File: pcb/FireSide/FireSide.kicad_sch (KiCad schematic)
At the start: 24 parts, among them J1 XT60-Male, J10 Screw_Terminal_Status_LED, J2 Spring_Terminal_Sensor_5V, J3 Spring_Terminal_Sensor_GND, J4 Screw_Terminal_Igniter_A, J5 Screw_Terminal_Igniter_B, J6 Spring_Terminal_A1toA3_SIG, J7 Spring_Terminal_A4toA6_SIG, J8 Spring_Terminal_A1toA3_GND, J9 Spring_Terminal_A4toA6_GND, Q1 BC557, Q2 IRLZ44N, Q3 BC557, Q4 IRLZ44N, Q5 2N2222, U1 LM7805ABV

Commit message: [FS] Create PCB Board Design
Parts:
- removed Q1, Q3: BC557, Package_TO_SOT_THT:TO-92_HandSolder, symbol Transistor_BJT:BC557
- removed Q5: 2N2222, Package_TO_SOT_THT:TO-92L_HandSolder, symbol Device:Q_NPN
- added Q1, Q3, Q5: 2N2222, Package_TO_SOT_THT:TO-92_HandSolder, symbol Transistor_BJT:PN2222A
- J1: footprint Connector_AMASS:AMASS_XT60-M_1x02_P7.20mm_Vertical -> XT60-M:AMASS_XT60-M
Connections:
- net +BATT: now also R2.1, R3.1
- net FIRE_PIN_A: now also Q1.2 (B)
- net FIRE_PIN_B: now also Q3.2 (B)
- net GND: now also Q1.1 (E), Q3.1 (E), Q5.1 (E); no longer R2.2, R3.2
- net STATUS_PIN: now also Q5.2 (B)
- net at Q2.1 (G): now also R2.2, Q1.3 (C); no longer R2.1
- net at Q4.1 (G): now also R3.2, Q3.3 (C); no longer R3.1
- net at R4.2: now also Q5.3 (C)
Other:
- moved on the sheet: R2

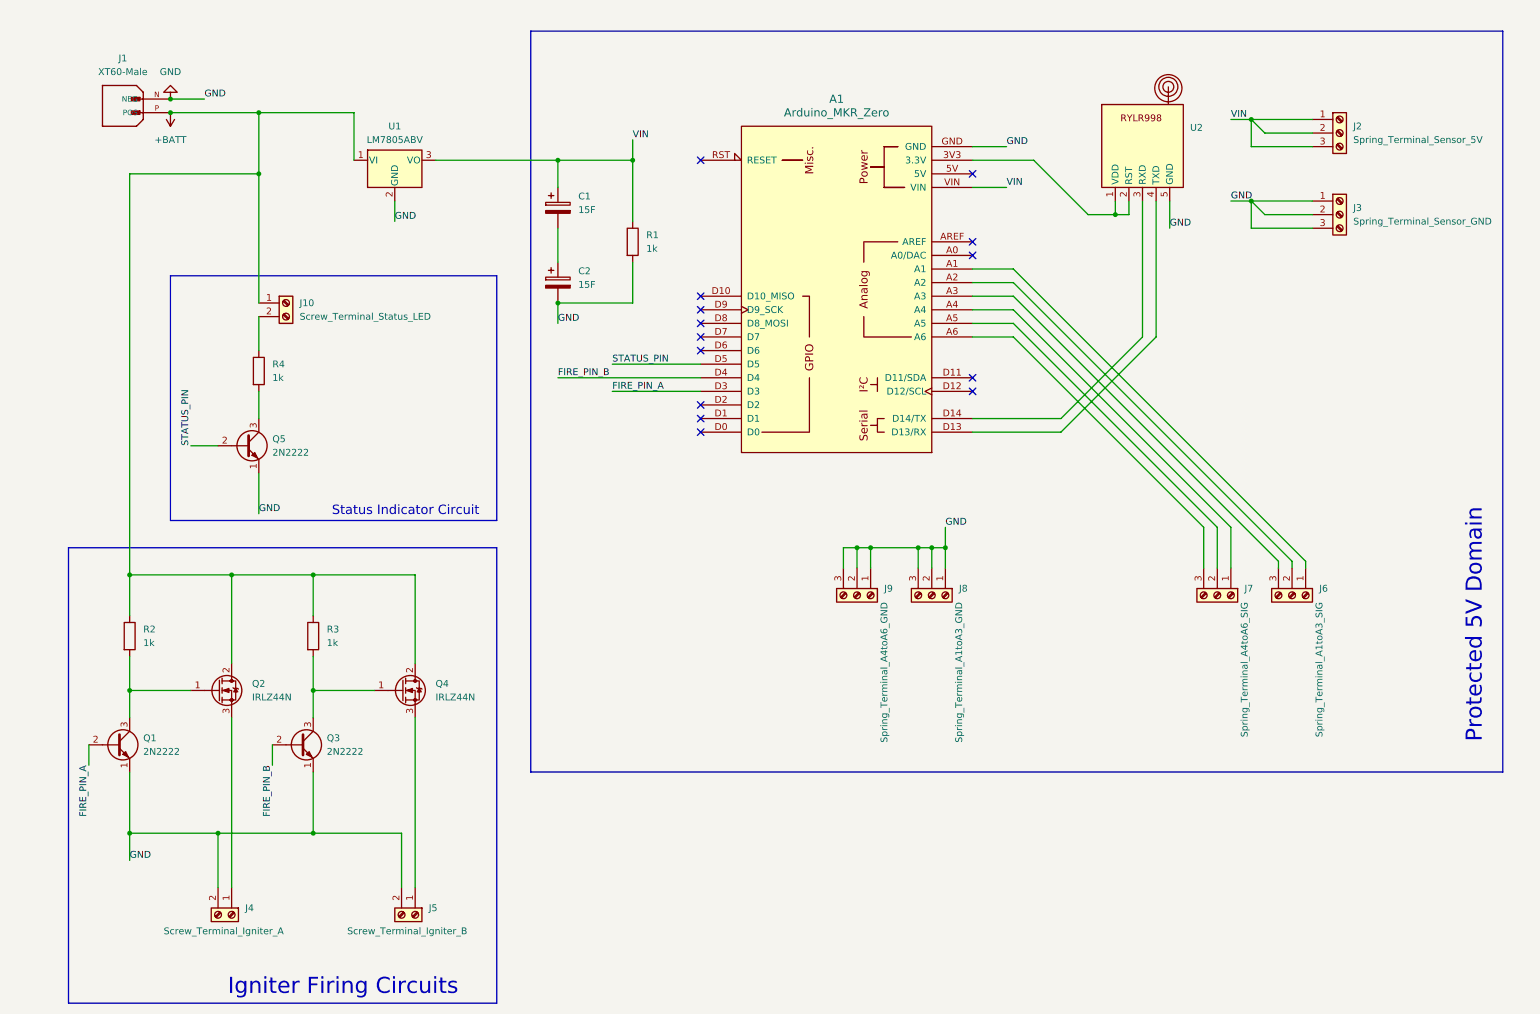
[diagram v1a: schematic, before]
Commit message: [FS] Update PCB to 120x80 mm and Use JST Connectors
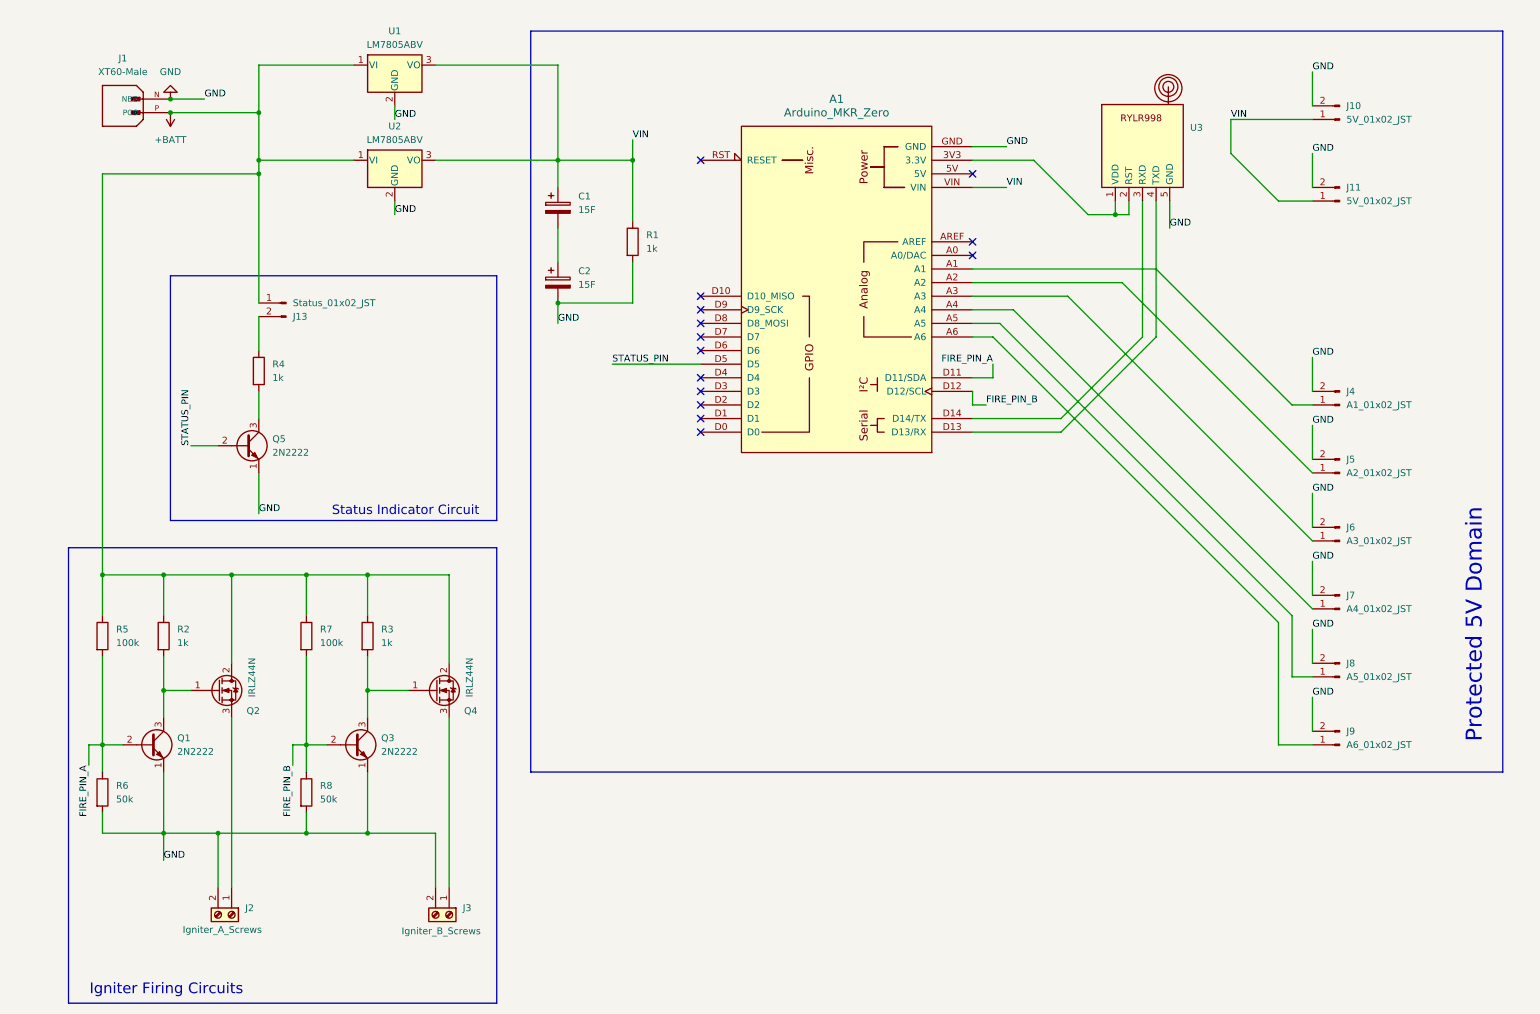
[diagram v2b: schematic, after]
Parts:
- removed J10: Screw_Terminal_Status_LED, TerminalBlock_MetzConnect:TerminalBlock_MetzConnect_Type059_RT06302HBWC_1x02_P3.50mm_Horizontal, symbol Connector:Screw_Terminal_01x02
- removed J2: Spring_Terminal_Sensor_5V, TerminalBlock_MetzConnect:TerminalBlock_MetzConnect_Type011_RT05503HBLC_1x03_P5.00mm_Horizontal, symbol Connector:Screw_Terminal_01x03
- removed J3: Spring_Terminal_Sensor_GND, TerminalBlock_MetzConnect:TerminalBlock_MetzConnect_Type011_RT05503HBLC_1x03_P5.00mm_Horizontal, symbol Connector:Screw_Terminal_01x03
- removed J6: Spring_Terminal_A1toA3_SIG, TerminalBlock_MetzConnect:TerminalBlock_MetzConnect_Type011_RT05503HBLC_1x03_P5.00mm_Horizontal, symbol Connector:Screw_Terminal_01x03
- removed J7: Spring_Terminal_A4toA6_SIG, TerminalBlock_MetzConnect:TerminalBlock_MetzConnect_Type011_RT05503HBLC_1x03_P5.00mm_Horizontal, symbol Connector:Screw_Terminal_01x03
- removed J8: Spring_Terminal_A1toA3_GND, TerminalBlock_MetzConnect:TerminalBlock_MetzConnect_Type011_RT05503HBLC_1x03_P5.00mm_Horizontal, symbol Connector:Screw_Terminal_01x03
- removed J9: Spring_Terminal_A4toA6_GND, TerminalBlock_MetzConnect:TerminalBlock_MetzConnect_Type011_RT05503HBLC_1x03_P5.00mm_Horizontal, symbol Connector:Screw_Terminal_01x03
- added J10, J11: 5V_01x02_JST, Connector_JST:JST_XH_B2B-XH-A_1x02_P2.50mm_Vertical, symbol Connector:Conn_01x02_Pin
- added J13: Status_01x02_JST, Connector_JST:JST_XH_B2B-XH-A_1x02_P2.50mm_Vertical, symbol Connector:Conn_01x02_Pin
- added J4: A1_01x02_JST, Connector_JST:JST_XH_B2B-XH-A_1x02_P2.50mm_Vertical, symbol Connector:Conn_01x02_Pin
- added J5: A2_01x02_JST, Connector_JST:JST_XH_B2B-XH-A_1x02_P2.50mm_Vertical, symbol Connector:Conn_01x02_Pin
- added J6: A3_01x02_JST, Connector_JST:JST_XH_B2B-XH-A_1x02_P2.50mm_Vertical, symbol Connector:Conn_01x02_Pin
- added J7: A4_01x02_JST, Connector_JST:JST_XH_B2B-XH-A_1x02_P2.50mm_Vertical, symbol Connector:Conn_01x02_Pin
- added J8: A5_01x02_JST, Connector_JST:JST_XH_B2B-XH-A_1x02_P2.50mm_Vertical, symbol Connector:Conn_01x02_Pin
- added J9: A6_01x02_JST, Connector_JST:JST_XH_B2B-XH-A_1x02_P2.50mm_Vertical, symbol Connector:Conn_01x02_Pin
- added R5, R7: 100k, Resistor_THT:R_Box_L8.4mm_W2.5mm_P5.08mm, symbol Device:R
- added R6, R8: 50k, Resistor_THT:R_Box_L8.4mm_W2.5mm_P5.08mm, symbol Device:R
- added U1: LM7805ABV, Package_TO_SOT_THT:TO-220-3_Horizontal_TabDown, symbol Regulator_Linear:LM7805_TO220
- J2: renamed from J4; value Screw_Terminal_Igniter_A -> Igniter_A_Screws
- J3: renamed from J5; value Screw_Terminal_Igniter_B -> Igniter_B_Screws
- Q1, Q3, Q5: footprint Package_TO_SOT_THT:TO-92_HandSolder -> Package_TO_SOT_THT:TO-92L_Wide
- renumbered U1 to U2, U2 to U3
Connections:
- net +BATT: now also J13.1 (Pin_1), R5.1, R7.1, U1.1 (VI)
- net FIRE_PIN_A: now also A1.D11 (D11/SDA), R5.2, R6.1; no longer A1.D3
- net FIRE_PIN_B: now also A1.D12 (D12/SCL), R7.2, R8.1; no longer A1.D4
- net GND: now also J10.2 (Pin_2), J11.2 (Pin_2), J4.2 (Pin_2), J5.2 (Pin_2), J6.2 (Pin_2), J7.2 (Pin_2), J8.2 (Pin_2), J9.2 (Pin_2), R6.2, R8.2, U1.2 (GND)
- net VIN: now also J10.1 (Pin_1), J11.1 (Pin_1), U1.3 (VO)
- net at R4.1: now also J13.2 (Pin_2)
- net at A1.A4: now also J7.1 (Pin_1)
- net at A1.A5: now also J8.1 (Pin_1)
- net at A1.A6: now also J9.1 (Pin_1)
- net at A1.A1: now also J4.1 (Pin_1)
- net at A1.A2: now also J5.1 (Pin_1)
- net at A1.A3: now also J6.1 (Pin_1)
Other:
- moved on the sheet: J3, Q1, Q3, Q4, R2, R3

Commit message: [FS] Transition PCB to Nucleo L412KB and SMD Components
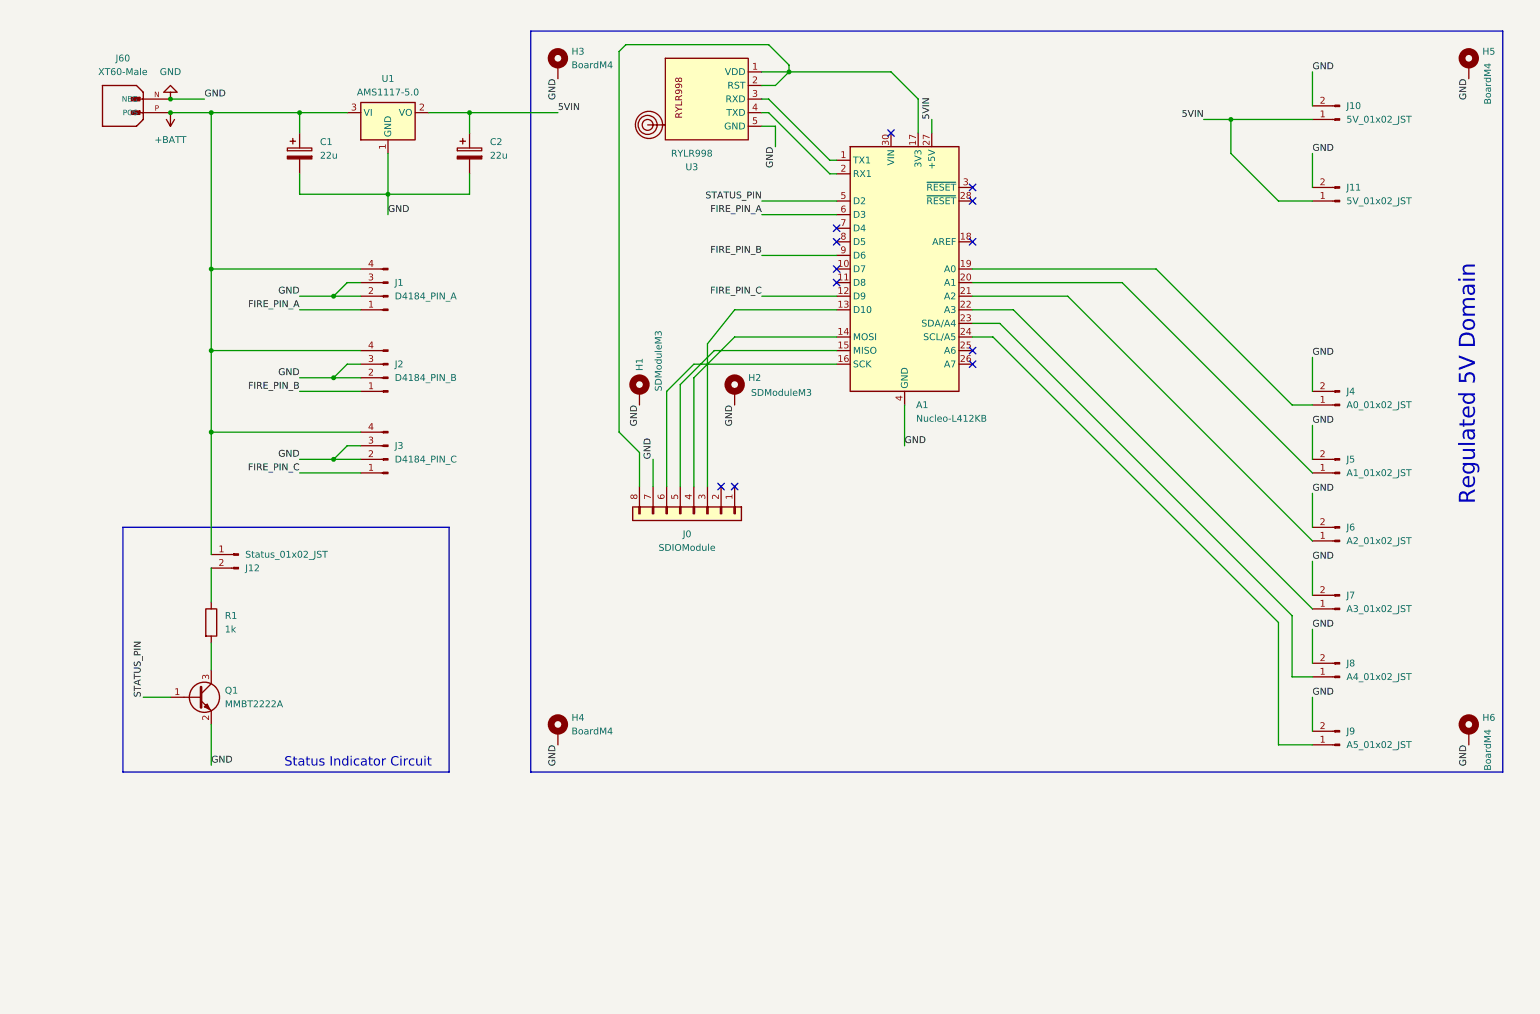
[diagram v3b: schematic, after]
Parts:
- removed A1: Arduino_MKR_Zero, PCM_arduino-library:Arduino_MKR_Zero_Socket, symbol PCM_arduino-library:Arduino_MKR_Zero_Socket
- removed J2: Igniter_A_Screws, TerminalBlock_MetzConnect:TerminalBlock_MetzConnect_Type059_RT06302HBWC_1x02_P3.50mm_Horizontal, symbol Connector:Screw_Terminal_01x02
- removed J3: Igniter_B_Screws, TerminalBlock_MetzConnect:TerminalBlock_MetzConnect_Type059_RT06302HBWC_1x02_P3.50mm_Horizontal, symbol Connector:Screw_Terminal_01x02
- removed Q1, Q3: 2N2222, Package_TO_SOT_THT:TO-92L_Wide, symbol Transistor_BJT:PN2222A
- removed Q2, Q4: IRLZ44N, Package_TO_SOT_THT:TO-220-3_Horizontal_TabDown, symbol Transistor_FET:IRLZ44N
- removed R1, R2, R3: 1k, Resistor_THT:R_Box_L8.4mm_W2.5mm_P5.08mm, symbol Device:R
- removed R5, R7: 100k, Resistor_THT:R_Box_L8.4mm_W2.5mm_P5.08mm, symbol Device:R
- removed R6, R8: 50k, Resistor_THT:R_Box_L8.4mm_W2.5mm_P5.08mm, symbol Device:R
- removed U2: LM7805ABV, Package_TO_SOT_THT:TO-220-3_Horizontal_TabDown, symbol Regulator_Linear:LM7805_TO220
- added A1: Nucleo-L412KB, Module:Arduino_Nano, symbol MCU_Module:Arduino_Nano_Every
- added H1, H2: SDModuleM3, MountingHole:MountingHole_3.2mm_M3_ISO7380_Pad_TopBottom, symbol Mechanical:MountingHole_Pad
- added H3, H4, H5, H6: BoardM4, MountingHole:MountingHole_4.3mm_M4_ISO7380_Pad_TopBottom, symbol Mechanical:MountingHole_Pad
- added J0: SDIOModule, Connector_Molex:Molex_Nano-Fit_105309-xx08_1x08_P2.50mm_Vertical, symbol Connector_Generic:Conn_01x08
- added J1: D4184_PIN_A, Connector_JST:JST_XH_B4B-XH-A_1x04_P2.50mm_Vertical, symbol Connector:Conn_01x04_Pin
- added J2: D4184_PIN_B, Connector_JST:JST_XH_B4B-XH-A_1x04_P2.50mm_Vertical, symbol Connector:Conn_01x04_Pin
- added J3: D4184_PIN_C, Connector_JST:JST_XH_B4B-XH-A_1x04_P2.50mm_Vertical, symbol Connector:Conn_01x04_Pin
- C1, C2: value 15F -> 22u; footprint Capacitor_THT:CP_Radial_D14.0mm_P5.00mm -> Capacitor_THT:CP_Radial_D5.0mm_P2.50mm
- J4: value A1_01x02_JST -> A0_01x02_JST
- J5: value A2_01x02_JST -> A1_01x02_JST
- J6: value A3_01x02_JST -> A2_01x02_JST
- J7: value A4_01x02_JST -> A3_01x02_JST
- J8: value A5_01x02_JST -> A4_01x02_JST
- J9: value A6_01x02_JST -> A5_01x02_JST
- Q1: renamed from Q5; value 2N2222 -> MMBT2222A; footprint Package_TO_SOT_THT:TO-92L_Wide -> Package_TO_SOT_SMD:SOT-23; symbol Transistor_BJT:PN2222A -> Transistor_BJT:MMBT2222A
- R1: renamed from R4; footprint Resistor_THT:R_Box_L8.4mm_W2.5mm_P5.08mm -> Resistor_SMD:R_0805_2012Metric_Pad1.20x1.40mm_HandSolder
- U1: value LM7805ABV -> AMS1117-5.0; footprint Package_TO_SOT_THT:TO-220-3_Horizontal_TabDown -> Package_TO_SOT_SMD:SOT-223-3_TabPin2; symbol Regulator_Linear:LM7805_TO220 -> Regulator_Linear:AMS1117-5.0
- U3: value ~ -> RYLR998
- renumbered J13 to J12, J1 to J60
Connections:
- net +BATT: now also C1.1, U1.3 (VI), J1.4 (Pin_4), J2.4 (Pin_4), J3.4 (Pin_4); no longer U1.1 (VI)
- net FIRE_PIN_A: now also A1.6 (D3), J1.1 (Pin_1)
- net FIRE_PIN_B: now also A1.9 (D6), J2.1 (Pin_1)
- net GND: now also C1.2, Q1.2 (E), U1.1 (GND), A1.29 (GND), A1.4 (GND), H1.1, H2.1, H3.1, H4.1, H5.1, H6.1, J0.7 (Pin_7), J1.2 (Pin_2), J1.3 (Pin_3), J2.2 (Pin_2), J2.3 (Pin_3), J3.2 (Pin_2), J3.3 (Pin_3); no longer Q1.1 (E), U1.2 (GND)
- net STATUS_PIN: now also Q1.1 (B), A1.5 (D2); no longer Q1.2 (B)
- net at J5.1 (Pin_1): now also A1.20 (A1)
- net at J7.1 (Pin_1): now also A1.22 (A3)
- net 5VIN: now reaches C2.1
- net 5VIN: now also J10.1 (Pin_1), J11.1 (Pin_1), U1.2 (VO), A1.27 (+5V); no longer C1.2
- net at J4.1 (Pin_1): now also A1.19 (A0)
- net at U3.1 (VDD), U3.2 (RST): now also A1.17 (3V3), J0.8 (Pin_8)
- net at J6.1 (Pin_1): now also A1.21 (A2)
- net at J8.1 (Pin_1): now also A1.23 (SDA/A4)
- net at J9.1 (Pin_1): now also A1.24 (SCL/A5)
- net at U3.4 (TXD): now also A1.2 (RX1)
- net at U3.3 (RXD): now also A1.1 (TX1)
- removed net VIN: C1.1, J10.1 (Pin_1), J11.1 (Pin_1), U1.3 (VO)
- new net: A1.13 (D10), J0.3 (Pin_3)
- new net: A1.14 (MOSI), J0.4 (Pin_4)
- new net: A1.15 (MISO), J0.5 (Pin_5)
- new net: A1.16 (SCK), J0.6 (Pin_6)
- new net FIRE_PIN_C: A1.12 (D9), J3.1 (Pin_1)
- no-connect marks 14 -> 12
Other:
- note added: "Regulated 5V Domain"
- note removed: "Igniter Firing Circuits"
- note removed: "Protected 5V Domain"
- moved on the sheet: J12, Q1, R1, U1, U3
